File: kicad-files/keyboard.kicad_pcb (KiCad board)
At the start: 2 copper layers, 350.2 x 100 mm, 187 parts, among them J1 TYPE-C-31-M12_13, Q1 2N7002, Q2 2N7002, SW1 K2-1187SQ-A4SW-06, T1 53261-0471, T2 53261-0471, U1 STM32F411CEU6, U2 USBLC6-2SC6, U3 AT24C256C-SSHL-T, U4 SGM2007-3.3XN5/TR, Y1 TAXM8M4RFDCET2T

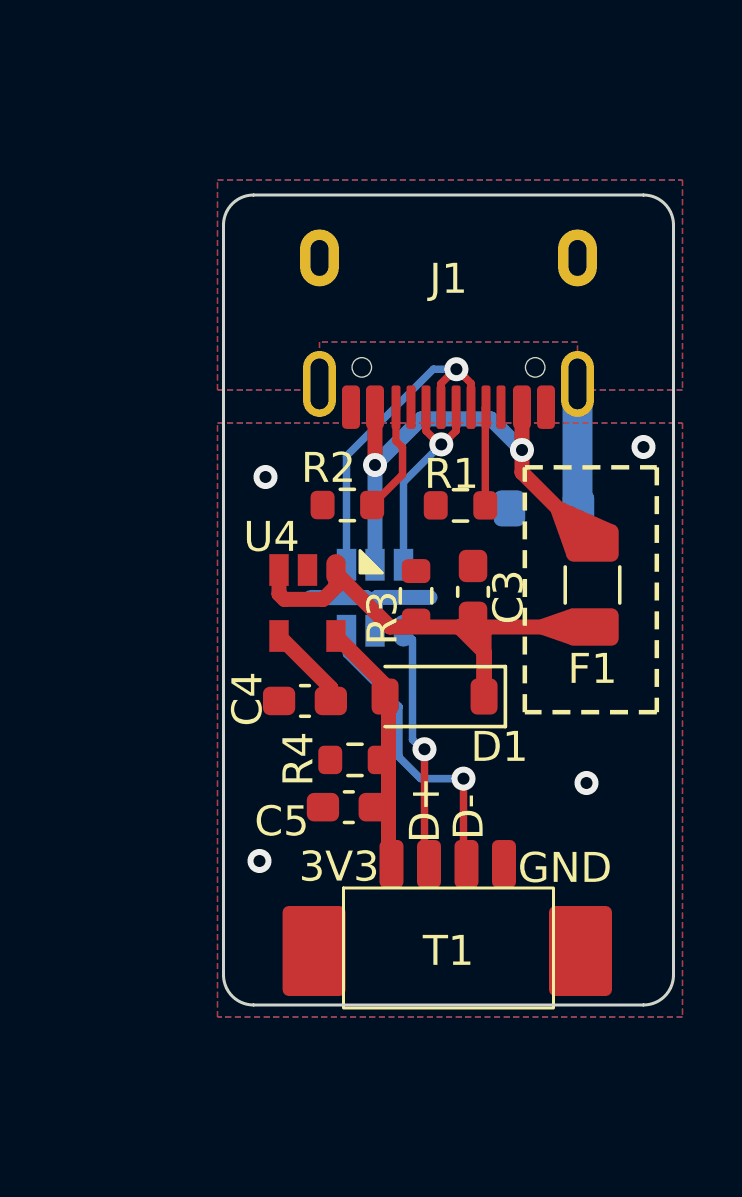
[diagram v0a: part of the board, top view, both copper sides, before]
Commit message: Added legshark logo to DB
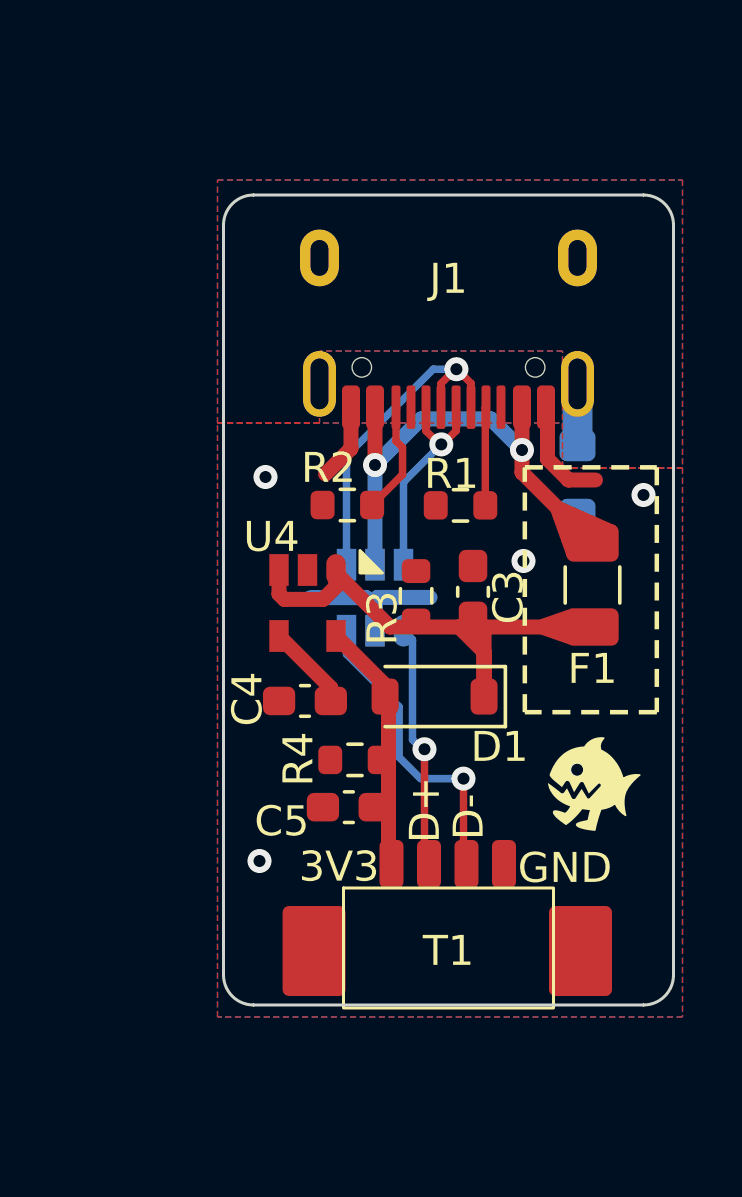
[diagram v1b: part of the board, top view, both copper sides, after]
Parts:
- added REF**: Legshark_Logo_SMall, Legshark:Legshark_Logo_SMall, F.Cu at (347.5, 54.6)
- moved FB1 1.46 mm to (347.0, 44.5), turned to -90 degrees
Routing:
- net GND1: track 5.98 -> 12.2 mm, vias 4 -> 5
- net GNDPWR: track 4.23 -> 2.00 mm

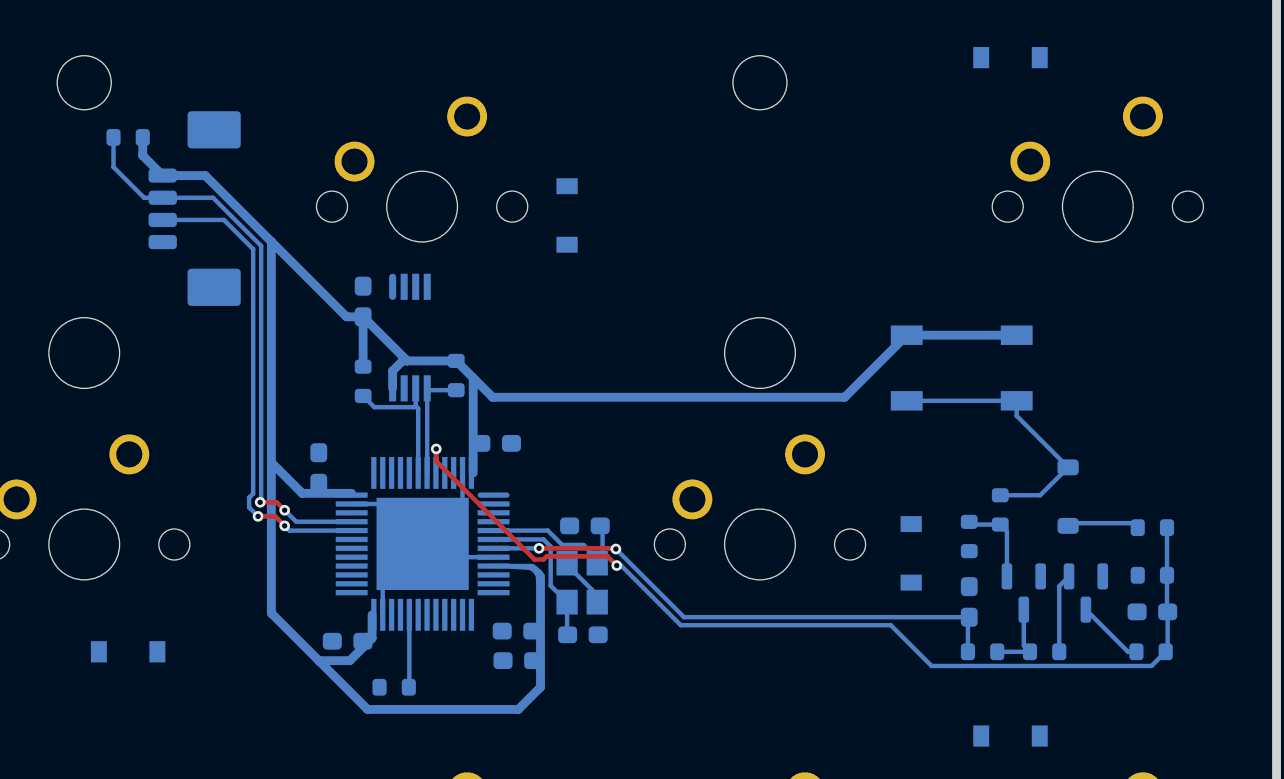
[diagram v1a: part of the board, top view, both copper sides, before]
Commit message: Rotated the molex header on the main board
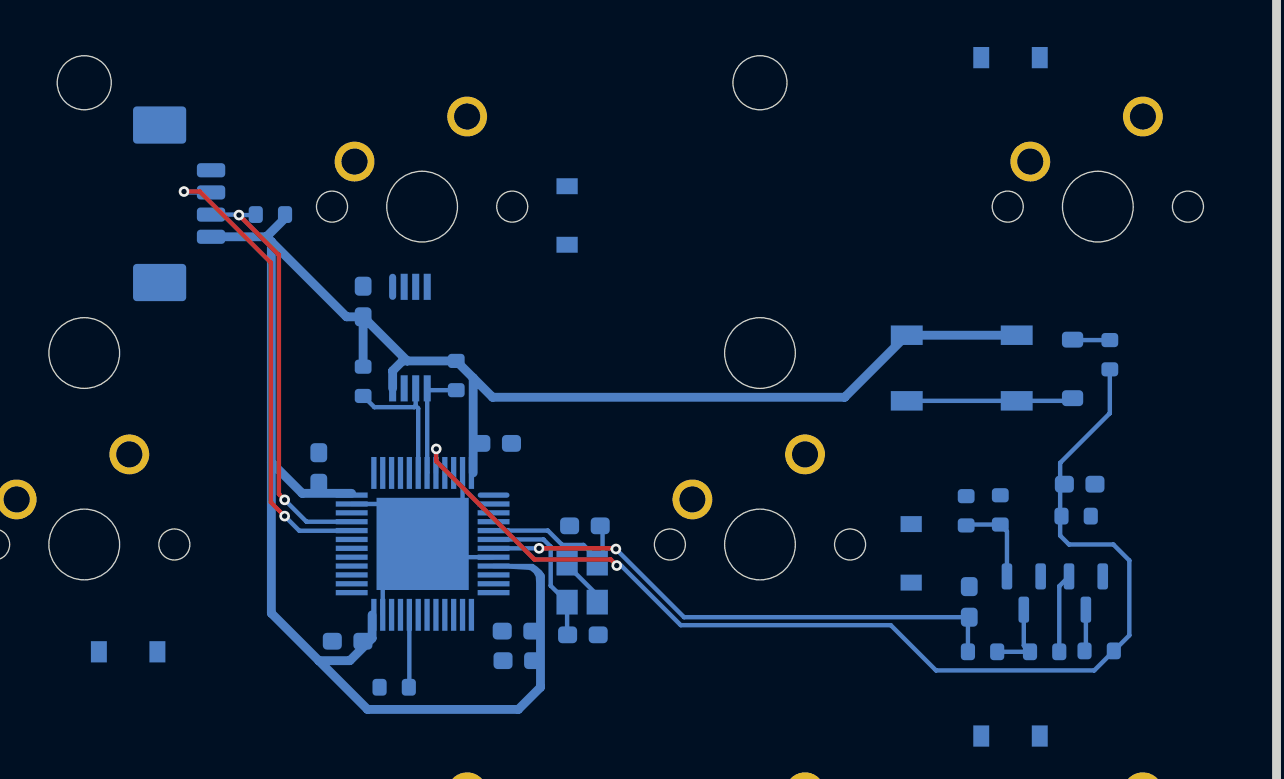
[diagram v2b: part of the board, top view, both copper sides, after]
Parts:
- moved R13 10.0 mm to (315.6, 58.5), turned to 90 degrees
- moved R5 9.12 mm to (268.3, 50.6)
- moved C8 8.29 mm to (313.9, 65.8), turned to 0 degrees
- moved D_72 7.20 mm to (313.5, 59.3), turned to -90 degrees
- moved R14 5.44 mm to (313.7, 67.6), turned to 0 degrees
- moved R15 2.93 mm to (315.0, 75.2)
- moved R10 1.46 mm to (307.5, 67.3), turned to 90 degrees
- moved T2 1.18 mm to (264.1, 50.0), turned to 90 degrees
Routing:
- net Net-(U1-BOOT0): track 55.8 -> 66.2 mm
- net D+: track 31.9 -> 24.0 mm
- net Net-(D_72-A): track 15.6 -> 9.41 mm
- net 3V3: track 125.9 -> 120.6 mm
- net Net-(D_72-K): track 4.09 -> 2.11 mm
- net Net-(Q2-D): track 3.83 -> 2.36 mm

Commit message: Resized MB again & started joining rows
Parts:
- removed REF**: Legshark_Logo_SMall, Legshark:Legshark_Logo_SMall
- added H1: Key, MountingHole:MountingHole_3.2mm_M3, F.Cu at (348.2, 39.0)
- moved D_31 15.1 mm to (314.9, 37.0)
- moved D_15 14.8 mm to (314.9, 17.8)
- moved C3 13.0 mm to (356.5, 48.2)
- moved C4 13.0 mm to (350.9, 51.9)
- moved C5 13.0 mm to (352.4, 55.4)
- moved D1 13.0 mm to (355.2, 51.7)
- moved F1 13.0 mm to (360.5, 48.0)
- moved FB1 13.0 mm to (360.0, 44.5)
- moved J1 13.0 mm to (355.7, 42.8)
- moved R1 13.0 mm to (356.1, 45.3)
- moved R2 13.0 mm to (352.3, 45.3)
- moved R3 13.0 mm to (354.6, 48.4)
- moved R4 13.0 mm to (352.6, 53.8)
- moved T1 13.0 mm to (355.7, 58.1)
- moved U2 13.0 mm to (353.2, 48.4)
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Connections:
- T1 pad : GND1 -> (no net)
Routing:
- net R4: track 0.00 -> 316.8 mm
- net Net-(D_31-A): track 0.00 -> 11.7 mm
- net Net-(D_15-A): track 0.00 -> 11.5 mm
- net Net-(D_9-A): track 0.00 -> 8.25 mm
- net Net-(D_65-A): track 0.00 -> 8.20 mm
- net Net-(D_64-A): track 0.00 -> 8.14 mm
- net Net-(D_44-A): track 0.00 -> 8.07 mm
- net Net-(D_42-A): track 0.00 -> 8.07 mm
- net Net-(D_40-A): track 0.00 -> 8.07 mm
- net Net-(D_39-A): track 0.00 -> 8.07 mm
- net Net-(D_8-A): track 0.00 -> 8.07 mm
- net Net-(D_7-A): track 0.00 -> 8.07 mm
- net Net-(D_29-A): track 0.00 -> 8.07 mm
- net Net-(D_28-A): track 0.00 -> 8.07 mm
- net Net-(D_27-A): track 0.00 -> 8.07 mm
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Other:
- board size 350.2 x 100 mm -> 361.7 x 94 mm

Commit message: Added legshark logo back
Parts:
- added Legshark_Logo1: Small, Legshark:Legshark_Logo_SMall, F.Cu at (360.5, 54.6)
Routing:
- net R3: track 0.00 -> 251.4 mm

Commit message: Started linking the front col
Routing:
- net R0: track 0.00 -> 339.6 mm
- net R1: track 0.00 -> 319.2 mm
- net R2: track 0.00 -> 264.3 mm
- net C2: track 0.00 -> 72.6 mm
- net C3: track 0.00 -> 72.3 mm
- net C4: track 0.00 -> 24.1 mm

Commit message: Routed more of the connections
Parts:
- moved D_59 7.96 mm to (266.0, 69.8), turned to 90 degrees
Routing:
- net C8: track 0.00 -> 93.4 mm
- net C10: track 0.00 -> 92.2 mm
- net C12: track 0.00 -> 92.0 mm
- net C5: track 0.00 -> 90.9 mm
- net C11: track 0.00 -> 90.6 mm
- net C15: track 0.00 -> 90.6 mm
- net C16: track 0.00 -> 88.5 mm
- net C0: track 0.00 -> 87.7 mm
- net C1: track 0.00 -> 74.6 mm
- net R3: track 251.4 -> 324.0 mm
- net C6: track 0.00 -> 69.0 mm
- net C7: track 0.00 -> 69.0 mm
- net C9: track 0.00 -> 69.0 mm
- net C13: track 0.00 -> 65.1 mm
- net C14: track 0.00 -> 61.2 mm
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
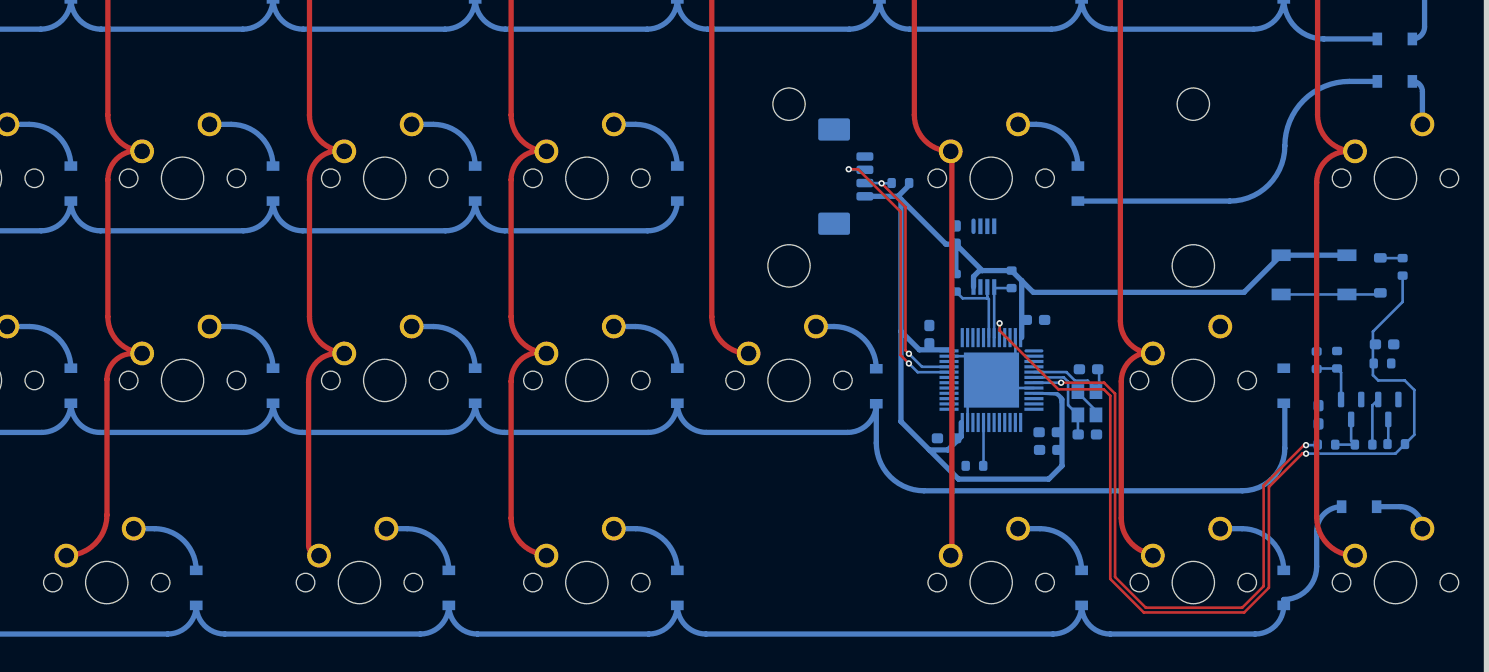
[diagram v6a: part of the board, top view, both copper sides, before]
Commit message: Moved some diodes around
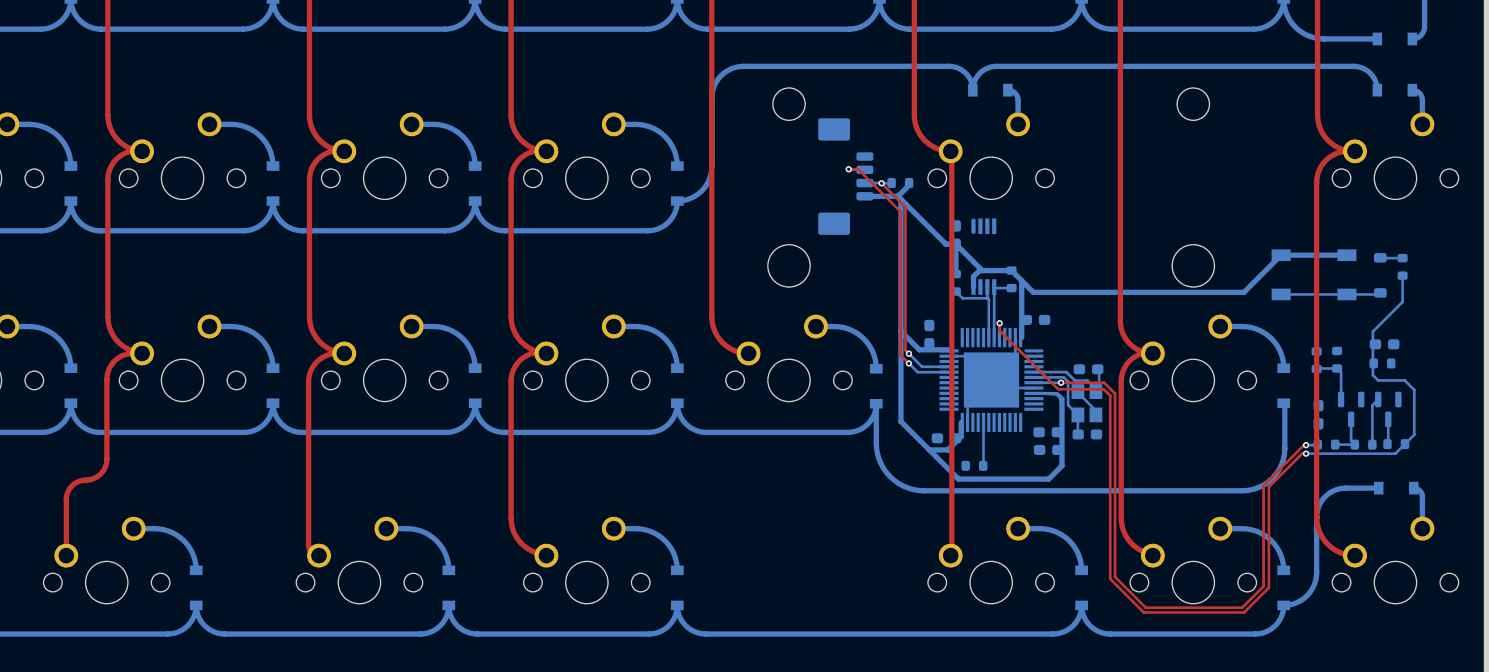
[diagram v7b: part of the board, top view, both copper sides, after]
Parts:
- moved D_45 12.1 mm to (276.8, 41.9), turned to 0 degrees
- moved D_71 3.91 mm to (315.0, 79.3)
- moved D_46 0.83 mm to (314.9, 41.9)
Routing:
- net R2: track 298.5 -> 343.6 mm
- net Net-(D_60-A): track 0.00 -> 8.07 mm
- net R4: track 316.8 -> 321.9 mm
- net Net-(D_45-A): track 7.72 -> 3.73 mm
- net Net-(D_71-A): track 5.41 -> 4.25 mm
- net Net-(D_46-A): track 4.55 -> 3.72 mm

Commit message: Started naming the switches
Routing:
- net GND: vias 0 -> 1
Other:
- board size 361.7 x 94 mm -> 361.7 x 100 mm
- board text added: "ALPHA_1"
- board text added: "ALPHA_2"
- board text added: "ALPHA_3"
- board text added: "ESCAPE"
- board text added: "TILDE"
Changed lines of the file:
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@@
     (property "ki_keywords" "R res resistor")
     (attr smd)
-    (fp_text reference "R14" (at 0.7 1.2) (layer "B.SilkS")
+    (fp_text reference "R14" (at 2.711632 0.094091) (layer "B.SilkS")
         (effects (font (size 1 1) (thickness 0.15)) (justify mirror))
     )
@@
     (property "ki_keywords" "R res resistor")
     (attr smd)
-    (fp_text reference "R5" (at 0.75 -1.25) (layer "B.SilkS")
+    (fp_text reference "R5" (at 1.729183 1.00311) (layer "B.SilkS")
         (effects (font (size 1 1) (thickness 0.15)) (justify mirror))
     )
@@
     (property "ki_keywords" "diode")
     (attr smd)
-    (fp_text reference "D_72" (at -0.1 -2.1 90) (layer "B.SilkS")
+    (fp_text reference "D_72" (at -3.2 0 -180) (layer "B.SilkS")
         (effects (font (size 1 1) (thickness 0.15)) (justify mirror))
     )
@@
     (property "ki_keywords" "R res resistor")
     (attr smd)
-    (fp_text reference "R8" (at 0 1.43 90) (layer "B.SilkS")
+    (fp_text reference "R8" (at 0.12661 -1.178834 90) (layer "B.SilkS")
         (effects (font (size 1 1) (thickness 0.15)) (justify mirror))
     )
@@
     (property "ki_keywords" "N-Channel Switching MOSFET")
     (attr smd)
-    (fp_text reference "Q2" (at 1.8125 1 -270) (layer "B.SilkS")
+    (fp_text reference "Q2" (at -2.074241 0.031461 -180) (layer "B.SilkS")
         (effects (font (size 1 1) (thickness 0.15)) (justify mirror))
     )
@@
     (property "ki_keywords" "I2C Serial EEPROM")
     (attr smd)
-    (fp_text reference "U3" (at 0 2.45 90) (layer "B.SilkS")
+    (fp_text reference "U3" (at -0.43419 -2.861892 -180) (layer "B.SilkS")
         (effects (font (size 1 1) (thickness 0.2)) (justify mirror))
     )
@@
     (property "Sheetname" "")
     (attr smd)
-    (fp_text reference "T2" (at 0 -2.1 270 unlocked) (layer "B.SilkS")
+    (fp_text reference "T2" (at -2.65 -5.125 unlocked) (layer "B.SilkS")
         (effects (font (size 1 1) (thickness 0.1)) (justify mirror))
     )
@@
         (effects (font (size 1 1) (thickness 0.1)) (justify left bottom mirror))
     )
-    (fp_text user "GND" (at 2.6 1.8 180 unlocked) (layer "B.SilkS")
+    (fp_text user "GND" (at 2.35 2.875 unlocked) (layer "B.SilkS")
         (effects (font (size 1 1) (thickness 0.1)) (justify left bottom mirror))
     )
-    (fp_text user "3V3" (at -1.7 1.7 180 unlocked) (layer "B.SilkS")
+    (fp_text user "3V3" (at -3.65 2.875 unlocked) (layer "B.SilkS")
         (effects (font (size 1 1) (thickness 0.1)) (justify left bottom mirror))
     )
@@
     (property "ki_keywords" "cap capacitor")
     (attr smd)
-    (fp_text reference "C6" (at 0 1.43 90) (layer "B.SilkS")
+    (fp_text reference "C6" (at 0.854146 -1.358269 90) (layer "B.SilkS")
         (effects (font (size 1 1) (thickness 0.15)) (justify mirror))
     )
@@
     (property "ki_keywords" "cap capacitor")
     (attr smd)
-    (fp_text reference "C9" (at 0.25 -1.5) (layer "B.SilkS")
+    (fp_text reference "C9" (at -1.237932 1.246108) (layer "B.SilkS")
         (effects (font (size 1 1) (thickness 0.15)) (justify mirror))
     )
@@
     (property "ki_keywords" "N-Channel Switching MOSFET")
     (attr smd)
-    (fp_text reference "Q1" (at 1.8125 1 -270) (layer "B.SilkS")
+    (fp_text reference "Q1" (at -2.193865 0.040409) (layer "B.SilkS")
         (effects (font (size 1 1) (thickness 0.15)) (justify mirror))
     )
@@
     (property "ki_keywords" "diode")
     (attr smd)
-    (fp_text reference "D_46" (at 3 0 90) (layer "B.SilkS")
+    (fp_text reference "D_46" (at -0.867655 1.75 180) (layer "B.SilkS")
         (effects (font (size 1 1) (thickness 0.15)) (justify mirror))
     )
@@
     (property "ki_keywords" "cap capacitor")
     (attr smd)
-    (fp_text reference "C12" (at 0 1.43) (layer "B.SilkS")
+    (fp_text reference "C12" (at -0.026771 -1.210358) (layer "B.SilkS")
         (effects (font (size 1 1) (thickness 0.15)) (justify mirror))
     )
@@
     (stroke (width 0.1) (type default)) (layer "Eco1.User"))
   (gr_line locked (start 0 50) (end 325 50)
-    (stroke (width 0.5) (type default)) (layer "Eco1.User"))
+    (stroke (width 0.1) (type default)) (layer "Eco1.User"))
   (gr_line locked (start 162.5 0) (end 162.5 100)
-    (stroke (width 0.5) (type default)) (layer "Eco1.User"))
+    (stroke (width 0.1) (type default)) (layer "Eco1.User"))
   (gr_line (start 348.2 61) (end 348.2 36)
     (stroke (width 0.1) (type default)) (layer "Edge.Cuts"))
@@
   (gr_line (start 362.2 62) (end 349.2 62)
     (stroke (width 0.1) (type default)) (layer "Edge.Cuts"))
-  (gr_rect (start 1.5 3.1) (end 323.5 97.1)
-    (stroke (width 0.5) (type default)) (fill none) (layer "Edge.Cuts"))
+  (gr_rect (start 1.5 -2.9) (end 323.5 97.1)
+    (stroke (width 0.25) (type default)) (fill none) (layer "Edge.Cuts"))
   (gr_arc (start 348.2 36) (mid 348.492893 35.292893) (end 349.2 35)
     (stroke (width 0.1) (type default)) (layer "Edge.Cuts"))
@@
   (gr_arc (start 362.2 35) (mid 362.907107 35.292893) (end 363.2 36)
     (stroke (width 0.1) (type default)) (layer "Edge.Cuts"))
-  (gr_text "HARD RESET" (at 311.75 55.25) (layer "B.SilkS")
+  (gr_text "HARD RESET" (at 311.5 55.25) (layer "B.SilkS")
+    (effects (font (size 0.9 0.9) (thickness 0.2) bold italic) (justify left bottom mirror))
+  )
+  (gr_text "ALPHA_1" (at 51 4.6) (layer "B.SilkS")
+    (effects (font (size 1 1) (thickness 0.15)) (justify left bottom mirror))
+  )
+  (gr_text "TILDE" (at 31 4.6) (layer "B.SilkS")
+    (effects (font (size 1 1) (thickness 0.15)) (justify left bottom mirror))
+  )
+  (gr_text "ALPHA_3" (at 89 4.6) (layer "B.SilkS")
+    (effects (font (size 1 1) (thickness 0.15)) (justify left bottom mirror))
+  )
+  (gr_text "ESCAPE" (at 12.5 4.6) (layer "B.SilkS")
+    (effects (font (size 1 1) (thickness 0.15)) (justify left bottom mirror))
+  )
+  (gr_text "ALPHA_2" (at 70 4.6) (layer "B.SilkS")
     (effects (font (size 1 1) (thickness 0.15)) (justify left bottom mirror))
   )
@@
   (segment (start 317.465 80.165) (end 317.465 83.17) (width 0.5) (layer "B.Cu") (net 72))
   (arc (start 316.65 79.35) (mid 317.226292 79.588708) (end 317.465 80.165) (width 0.5) (layer "B.Cu") (net 72))
+  (via (at 276.854919 69.166315) (size 0.6) (drill 0.3) (layers "F.Cu" "B.Cu") (free) (net 104))
   (segment (start 274.604919 66.916315) (end 276.854919 69.166315) (width 0.25) (layer "B.Cu") (net 104))
   (segment (start 279.104919 66.916315) (end 276.854919 69.166315) (width 0.25) (layer "B.Cu") (net 104))
